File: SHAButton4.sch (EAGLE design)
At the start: 5 parts, among them SW1 SWITCH-SPDT-ILLUMINATED, SW2 SWITCH-SPDT-ILLUMINATED, SW3 SWITCH-SPDT-ILLUMINATED, SW4 SWITCH-SPDT-ILLUMINATED

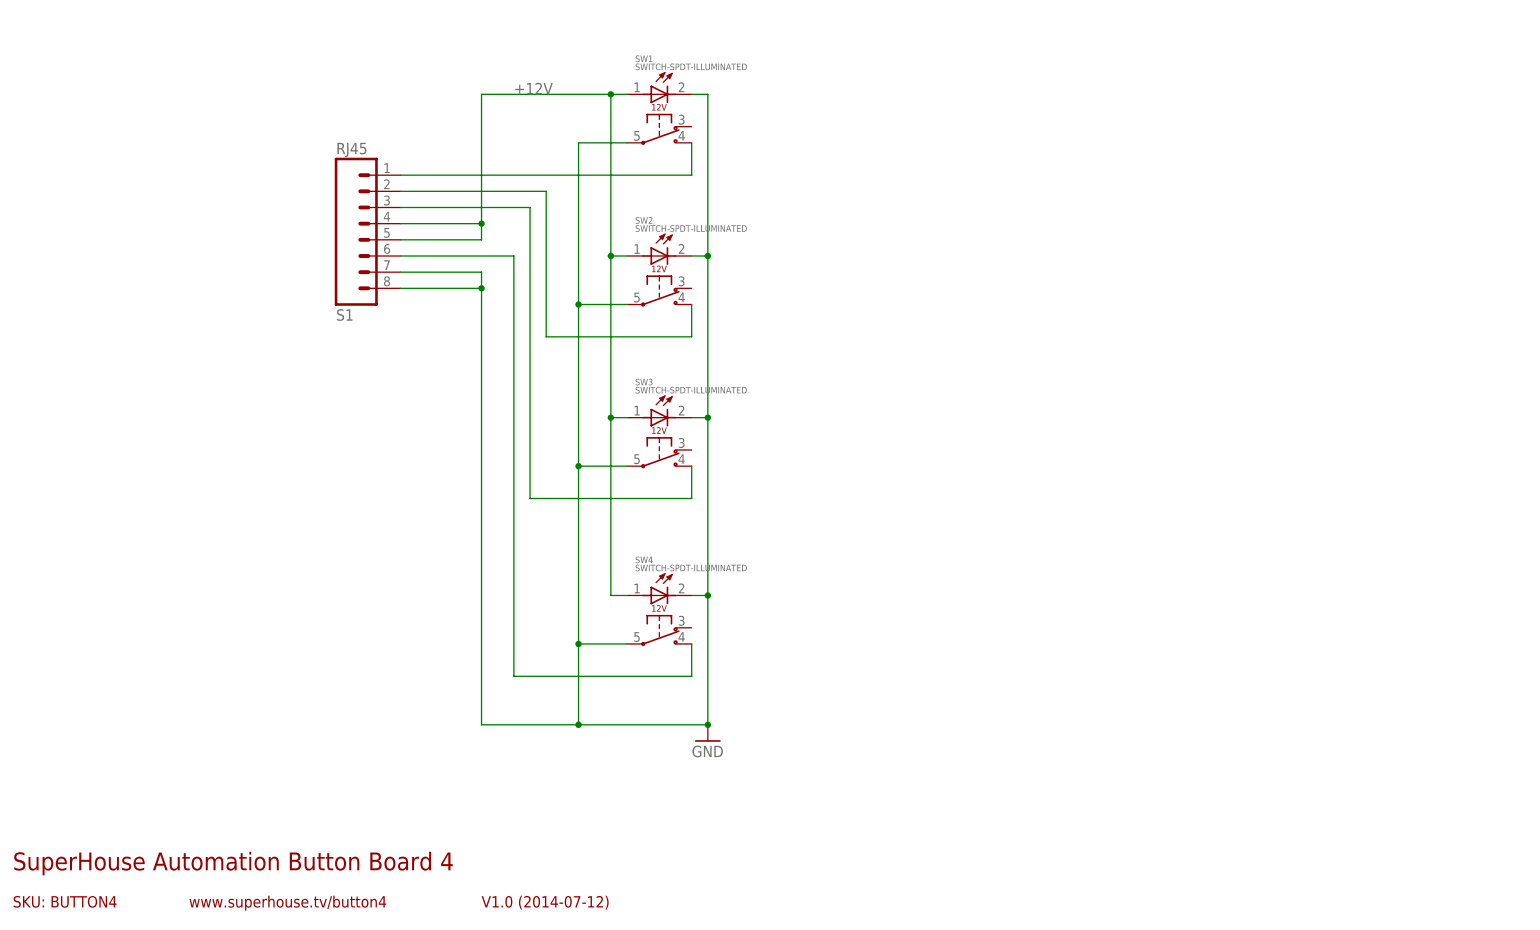
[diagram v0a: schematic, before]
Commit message: Improved labels for clarity
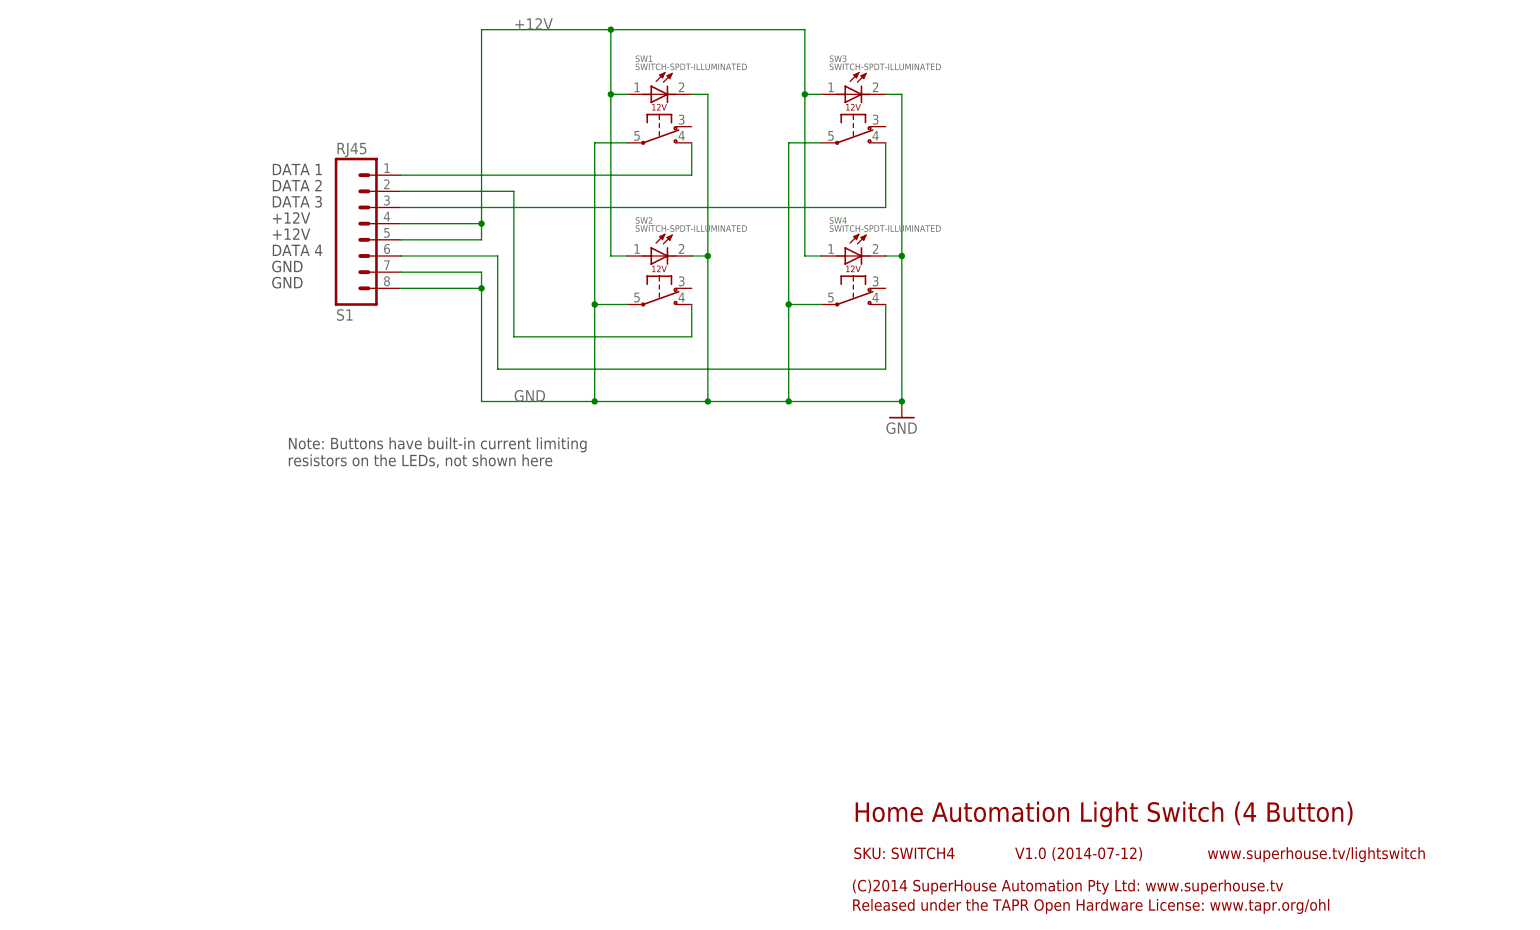
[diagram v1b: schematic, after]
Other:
- note added: "(C)2014 SuperHouse Automation Pty Ltd: www.superhouse.tv"
- note added: "+12V"
- note added: "DATA 1"
- note added: "DATA 2"
- note added: "DATA 3"
- note added: "DATA 4"
- note added: "GND"
- note added: "Home Automation Light Switch (4 Button)"
- note added: "Note: Buttons have built-in current limiting resistors on the LEDs, not shown here"
- note added: "Released under the TAPR Open Hardware License: www.tapr.org/ohl"
- note added: "SKU: SWITCH4"
- note added: "www.superhouse.tv/lightswitch"
- note removed: "SKU: BUTTON4"
- note removed: "SuperHouse Automation Button Board 4"
- note removed: "www.superhouse.tv/button4"
- moved on the sheet: SW3, SW4

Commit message: Replaced buttons with more common SPST type
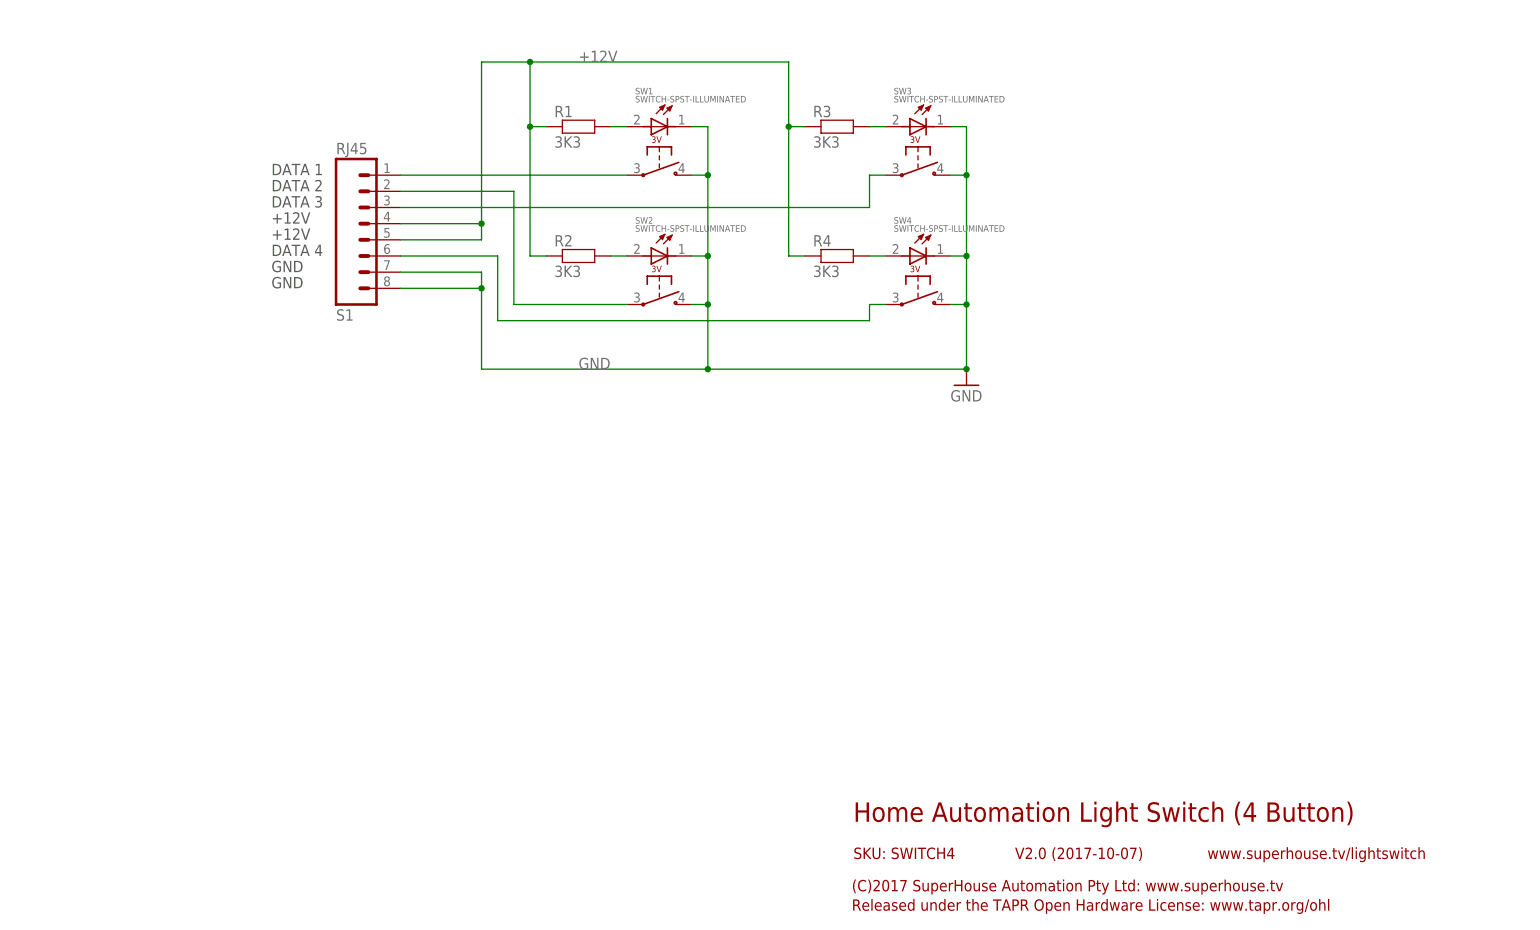
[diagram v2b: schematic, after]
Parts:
- added R1, R2, R3, R4: 3K3, freetronics-jon:RESISTOR0603
- SW1, SW2, SW3, SW4: value SWITCH-SPDT-ILLUMINATED -> SWITCH-SPST-ILLUMINATED; device freetronics-jon:SWITCH-SPDT-ILLUMINATED -> freetronics-jon:SWITCH-SPST-ILLUMINATED
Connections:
- new net N$1: R2.2, SW2.+
- new net N$6: R1.2, SW1.+
- new net N$7: R3.2, SW3.+
- new net N$8: R4.2, SW4.+
- net +12V: now also R1.1, R2.1, R3.1, R4.1; no longer SW1.+, SW2.+, SW3.+, SW4.+
- net GND: now also SW1.NO, SW2.NO, SW3.NO, SW4.NO; no longer SW1.COM, SW2.COM, SW3.COM, SW4.COM
- net N$2: now also SW3.COM; no longer SW3.NO
- net N$3: now also SW4.COM; no longer SW4.NO
- net N$4: now also SW1.COM; no longer SW1.NO
- net N$5: now also SW2.COM; no longer SW2.NO
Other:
- note added: "(C)2017 SuperHouse Automation Pty Ltd: www.superhouse.tv"
- note added: "V2.0 (2017-10-07)"
- note removed: "(C)2014 SuperHouse Automation Pty Ltd: www.superhouse.tv"
- note removed: "Note: Buttons have built-in current limiting resistors on the LEDs, not shown here"
- note removed: "V1.0 (2014-07-12)"
